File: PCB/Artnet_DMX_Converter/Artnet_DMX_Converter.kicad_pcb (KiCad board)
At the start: 4 copper layers, 100 x 100 mm, 255 parts, among them IC1 NPM1300-QEAA-R7, J1 Conn_01x03_MountingPin, J10 XLR5, J11 XLR3, J12 IDC, J13 Conn_02x04, J2 USB_C_Receptacle_USB2.0_14P, J3 RJ45, J4 XLR5, J5 XLR3, J6 XLR5, J7 XLR3, J8 XLR5, J9 XLR3, SW1 SW_Push, SW2 SW_Push, T1 FA2805, U1 RP2350B, U10 MAX3485, U11 MAX3485, U12 TXS0101DCK, U2 W25Q128JVS, U3 USBLC6-2SC6, U4 W5500, U5 VO618A-3X019T, U6 SI3402-B-GMR, U7 TLV431, U8 MAX3485, U9 MAX3485, Y1 ABM8-272-T3, Y2 ABM8-25.000MHZ-10-D1G-T

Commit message: EVEN MORE PCB updates
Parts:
- added G***: LOGO, Art:Flag-standalone, F.Cu at (78.8, 81.2)
- TP12, TP13, TP3: moved to B.Cu
- moved TP3 2.34 mm to (53.2, 94.4)
- moved TP14 1.53 mm to (94.6, 79.4)
- moved TP13 0.92 mm to (92.5, 107.7)
- moved TP12 0.60 mm to (70.6, 85.2)
- moved TP4 0.20 mm to (51.9, 97.1)
- moved TP5 0.20 mm to (48.9, 97.1)
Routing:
- net /Display/BACKLIGHT: track 15.2 -> 17.5 mm
- net /Microcontroller/FLASH_SS: track 5.26 -> 5.99 mm, vias 0 -> 1
- net Net-(D10-A): track 12.5 -> 13.1 mm, vias 0 -> 1

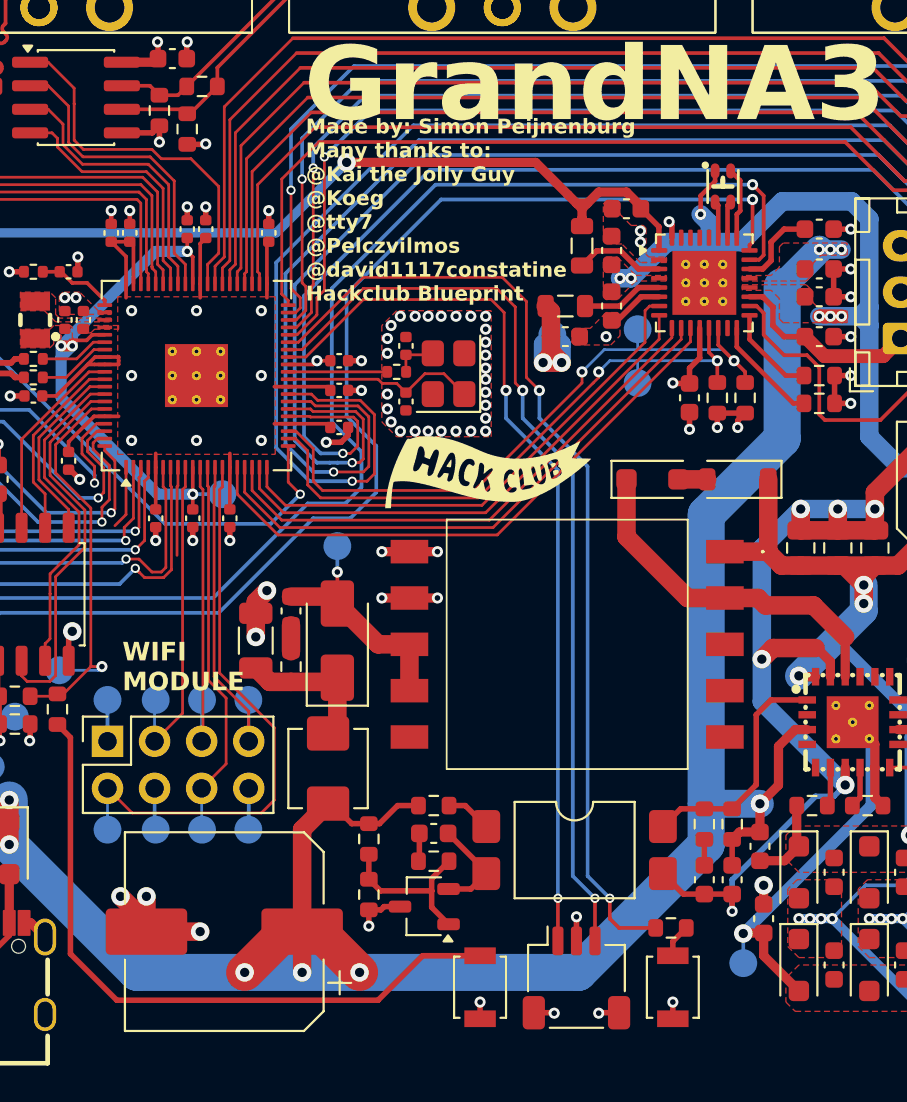
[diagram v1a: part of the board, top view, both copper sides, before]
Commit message: Fixed allot of problems
Added a new LDO for the 3.3V rail to support the load i miscalculated 💀
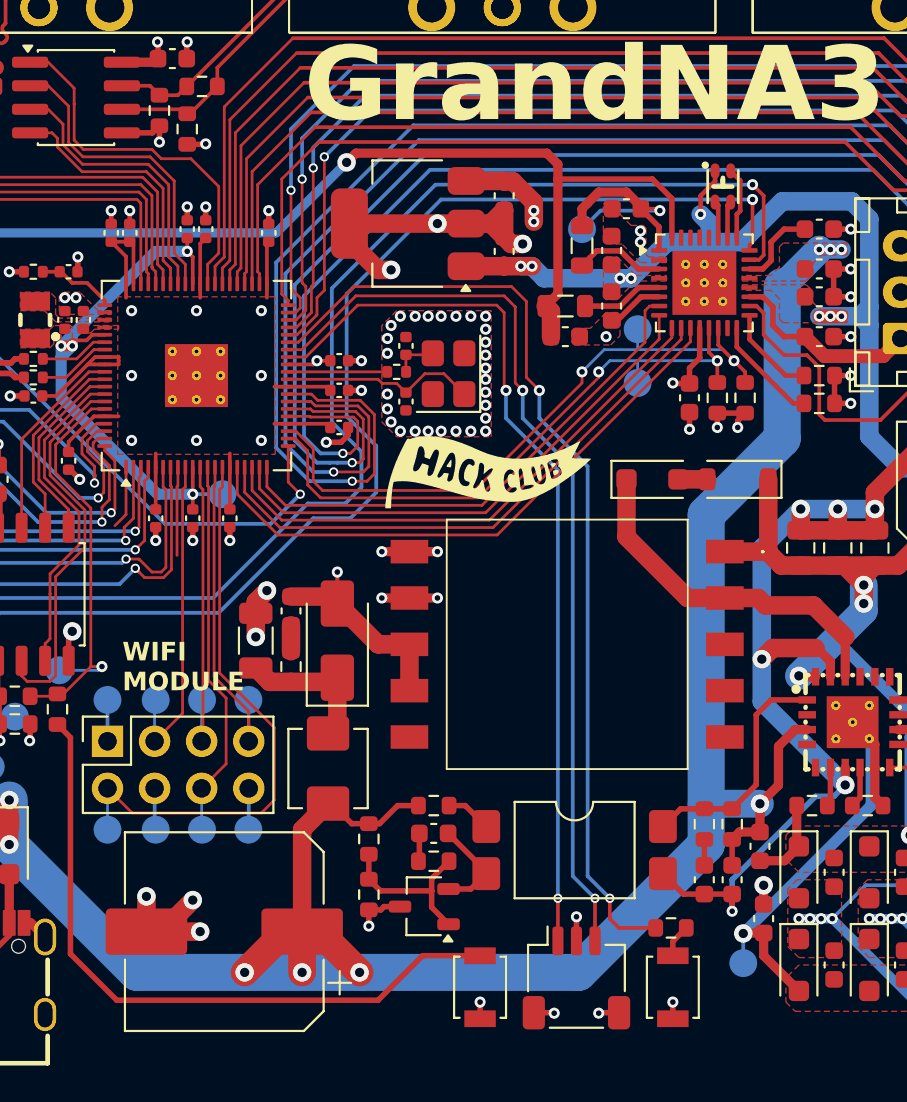
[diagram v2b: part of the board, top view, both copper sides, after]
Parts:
- added C89: 10u, Capacitor_SMD:C_0603_1608Metric, F.Cu at (79.6, 69.3)
- added C90: 10u, Capacitor_SMD:C_0603_1608Metric, F.Cu at (79.6, 66.3)
- added U13: AP7361C-33E, Package_TO_SOT_SMD:SOT-223-3_TabPin2, F.Cu at (74.4, 67.8)
- moved G*** 10.9 mm to (94.0, 78.9), turned to -90 degrees
- moved TP14 6.70 mm to (94.6, 72.7)
- moved TP16 5.92 mm to (83.8, 68.1)
- moved TP12 3.10 mm to (70.6, 88.3)
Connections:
- net +LED renamed +LDO
- C86 pad 1: +DISPLAY -> Net-(IC1-VOUT1)
- C87 pad 1: +3V3 -> +DISPLAY
- IC1 pad 1: +DISPLAY -> Net-(IC1-VOUT1)
- IC1 pad 32: +3V3 -> +DISPLAY
- L4 pad 1: +DISPLAY -> Net-(IC1-VOUT1)
- L5 pad 1: +3V3 -> +DISPLAY
- TP16 pad 1: +3V3 -> Net-(IC1-VOUT1)
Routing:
- net GND: track 140.0 -> 157.3 mm, vias 155 -> 158
- net Net-(IC1-VOUT1): track 0.00 -> 13.7 mm, vias 0 -> 1
- net +LDO: track 296.8 -> 306.0 mm, vias 17 -> 19
- net +DISPLAY: track 58.5 -> 66.4 mm
- net +3V3: track 114.8 -> 109.5 mm, vias 38 -> 37

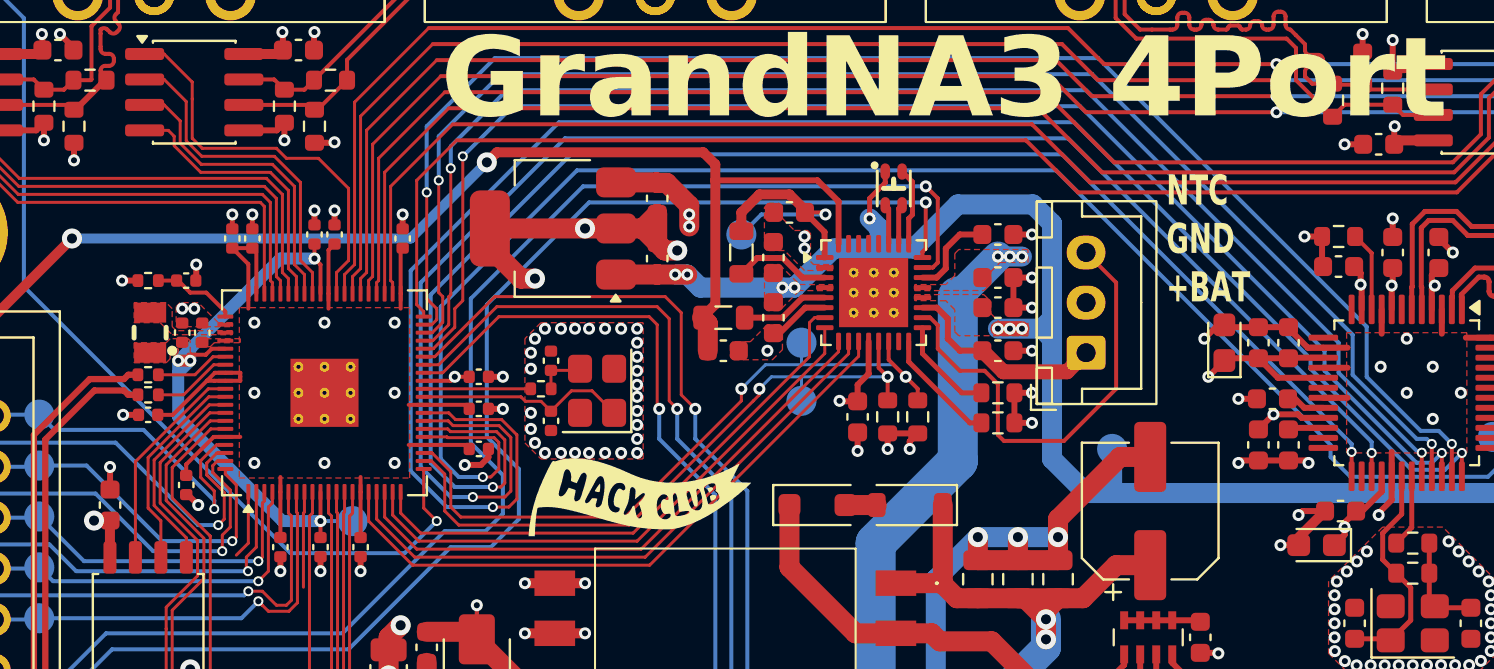
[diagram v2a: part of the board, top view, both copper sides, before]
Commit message: Fixed RP2350 power layout
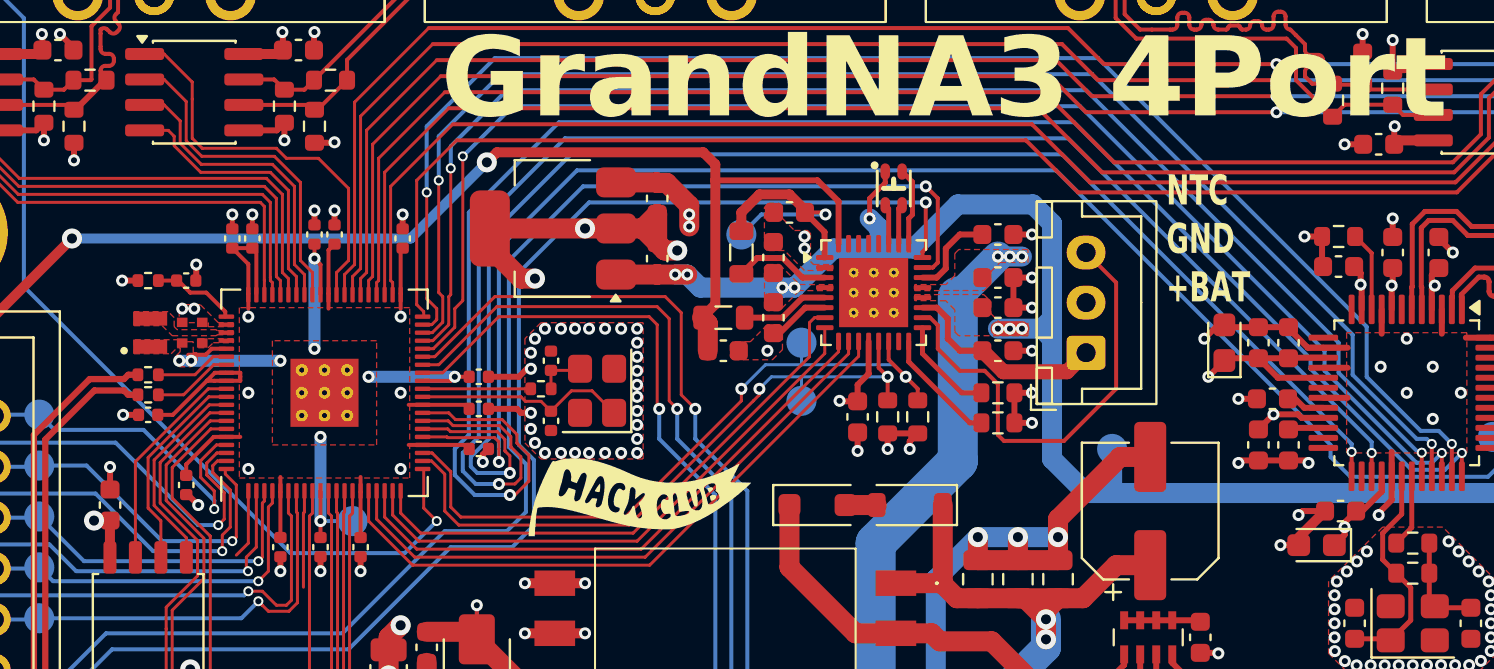
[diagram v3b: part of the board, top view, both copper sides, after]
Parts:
- removed ? (x9): , 
- C15, C16: footprint Capacitor_SMD:C_0402_1005Metric -> RP2350_80QFN_minimal:C_0402_1005Metric_small_pads
- L1: footprint LCSC:IND-SMD_L2.0-W1.6_AOTA-B201610S3R3-101-T -> RP2350_80QFN_minimal:L_pol_2016
- U1: footprint Package_DFN_QFN:QFN-80-1EP_10x10mm_P0.4mm_EP3.4x3.4mm -> RP2350_80QFN_minimal:RP2350-QFN-80-1EP_10x10_P0.4mm_EP3.4x3.4mm_ThermalVias
- turned L1 to 90 degrees
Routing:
- net +1V1: track 45.0 -> 28.8 mm, vias 5 -> 9
- net /Ethernet/RST: track 85.0 -> 80.2 mm
- net /Ethernet/LINKLED: track 75.5 -> 72.3 mm
- net /Ethernet/INTERRUPT: track 89.0 -> 85.9 mm
- net /Ethernet/ACTLED: track 80.2 -> 77.2 mm
- net GND: track 157.3 -> 159.4 mm, vias 158 -> 156
- net +3V3: vias 37 -> 35

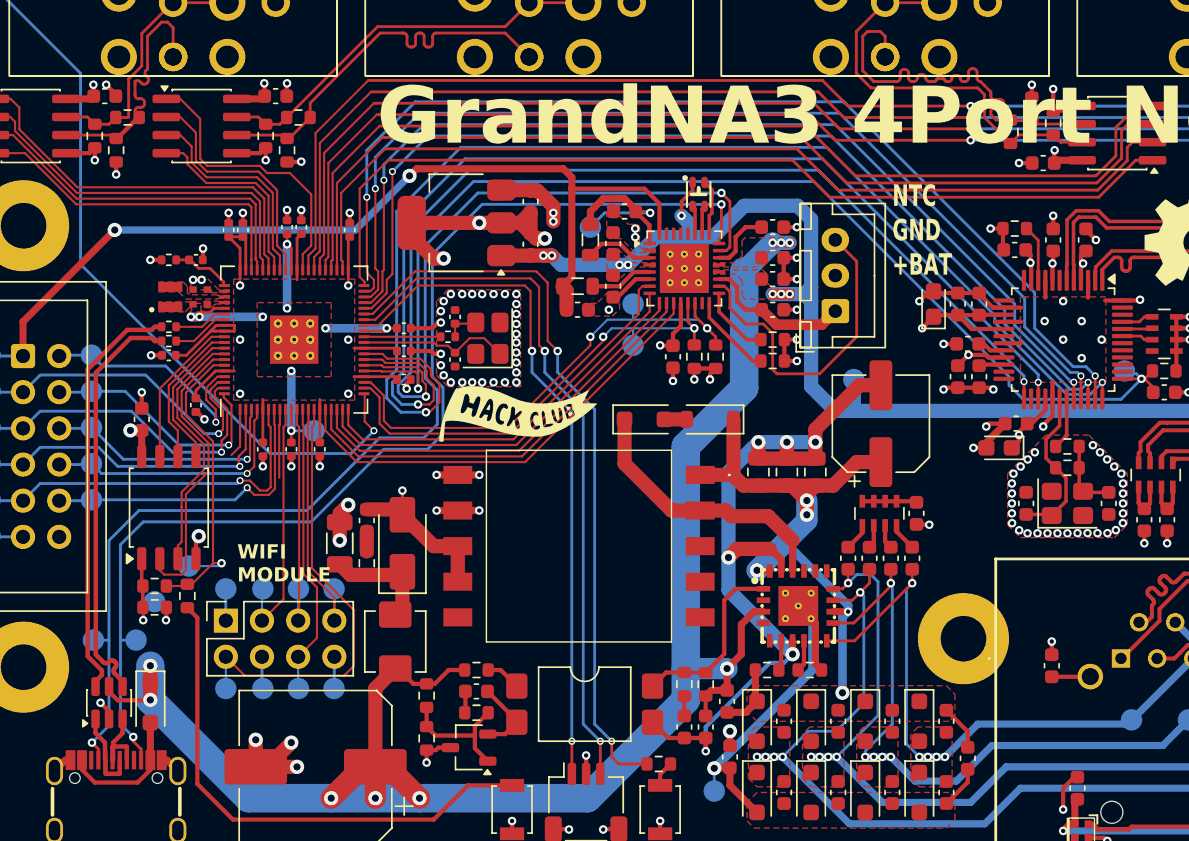
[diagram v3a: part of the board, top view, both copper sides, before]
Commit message: Testpoints and GND1 Fill
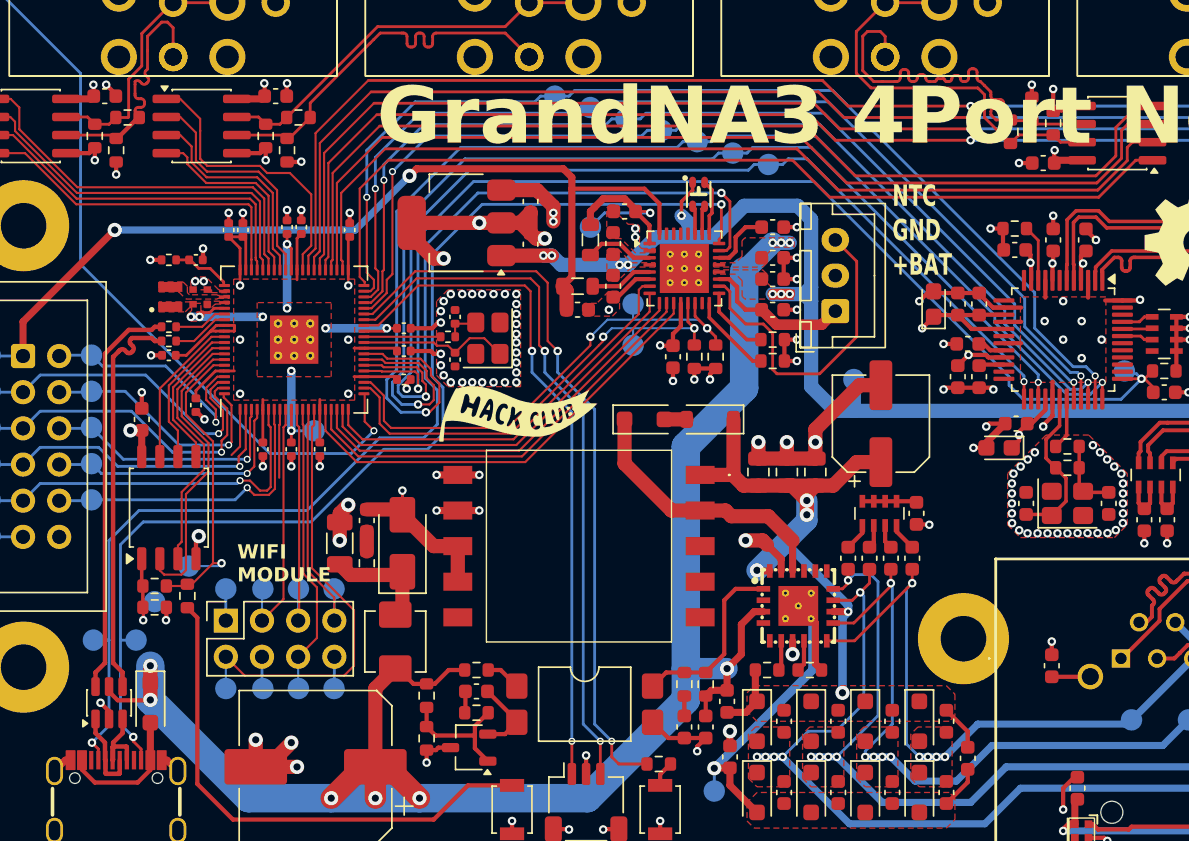
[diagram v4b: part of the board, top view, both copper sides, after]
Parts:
- added TP11: TestPoint, TestPoint:TestPoint_Pad_D1.5mm, B.Cu at (86.3, 60.5)
- added TP12: TestPoint, TestPoint:TestPoint_Pad_D1.5mm, B.Cu at (83.8, 59.7)
- added TP13: TestPoint, TestPoint:TestPoint_Pad_D1.5mm, B.Cu at (88.8, 61.3)
- added TP14: TestPoint, TestPoint:TestPoint_Pad_D1.5mm, B.Cu at (81.3, 58.9)
- added TP15: TestPoint, TestPoint:TestPoint_Pad_D1.5mm, B.Cu at (91.3, 62.1)
- added TP16: TestPoint, TestPoint:TestPoint_Pad_D1.5mm, B.Cu at (96.3, 63.7)
- added TP17: TestPoint, TestPoint:TestPoint_Pad_D1.5mm, B.Cu at (93.8, 62.9)
- renumbered C81 to C80, C82 to C81, C83 to C82, C84 to C83, C80 to C84, TP11 to TP18, TP12 to TP19, TP13 to TP20, TP15 to TP21, TP14 to TP22, TP16 to TP23, TP17 to TP24, TP18 to TP25, TP19 to TP26, TP20 to TP27, TP21 to TP28, TP22 to TP29, TP23 to TP30, TP24 to TP31, TP25 to TP32, TP26 to TP33, TP27 to TP34, TP28 to TP35, TP29 to TP36, TP30 to TP37, TP31 to TP38, TP32 to TP39, TP33 to TP40, TP34 to TP41, TP35 to TP42, TP36 to TP43, TP37 to TP44
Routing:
- net GND1: track 56.9 -> 24.4 mm
- net /Ethernet/V-: track 38.2 -> 27.0 mm
- net /USB/USB_D+: track 29.3 -> 28.4 mm
- net /USB/USB_D-: track 29.3 -> 28.4 mm
- net /Ethernet/MISO: track 69.9 -> 70.6 mm
- net /Ethernet/SCS: track 69.7 -> 70.3 mm
- net /Ethernet/SCK: track 71.8 -> 72.4 mm
- net /Ethernet/MOSI: track 74.2 -> 74.9 mm
- net /Ethernet/INTERRUPT: track 85.9 -> 86.5 mm
- net /Ethernet/LINKLED: track 72.3 -> 73.0 mm
- net /Ethernet/ACTLED: track 77.2 -> 77.8 mm
- added copper zone on B.Cu, net /Ethernet/V-
- added copper zone on In2.Cu, net GND1
